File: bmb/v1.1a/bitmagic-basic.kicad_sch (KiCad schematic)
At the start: 39 parts, among them IC1 CY7C68013A-56, J1 Conn, J2 USB_C_Receptacle_USB2.0, U1 3.3V, U2 USBLC6-2, U3 IP425x-4-TTL, U4 IP425x-4-TTL, U5 24LC00, U6 IP425x-4-TTL, X1 24MHz

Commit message: bmb: Updated manufacturing data.
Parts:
- C14: Key cap-cer-0401-1u -> cap-cer-0402-1u
- D1: MFN (none) -> ORH-G36A; Manufacturer (none) -> Orient
- IC1: MFN (none) -> CY768013A-56; Manufacturer (none) -> Cypress
- J2: Key (none) -> conn-smd-usb-c-2; MFN (none) -> TYPE-C-31-M-12; Manufacturer (none) -> Korean Horoparts; Source (none) -> ANY
- R1: value 330E -> 2k7; Key res-0402-330 -> res-0402-2k7
- U1: MFN (none) -> SPX3819M5-L-3-3/TR; Manufacturer (none) -> MaxLinear
- U2: MFN (none) -> USBLC6-2P6; Manufacturer (none) -> STM
- U3, U4, U6: MFN (none) -> IP4254CZ8-4-TTL; Manufacturer (none) -> Nexperia
- U5: MFN (none) -> 24LC00T-I/OT; Manufacturer (none) -> Microchip
- X1: MFN (none) -> JF4024M00009T8188070; Manufacturer (none) -> JWT

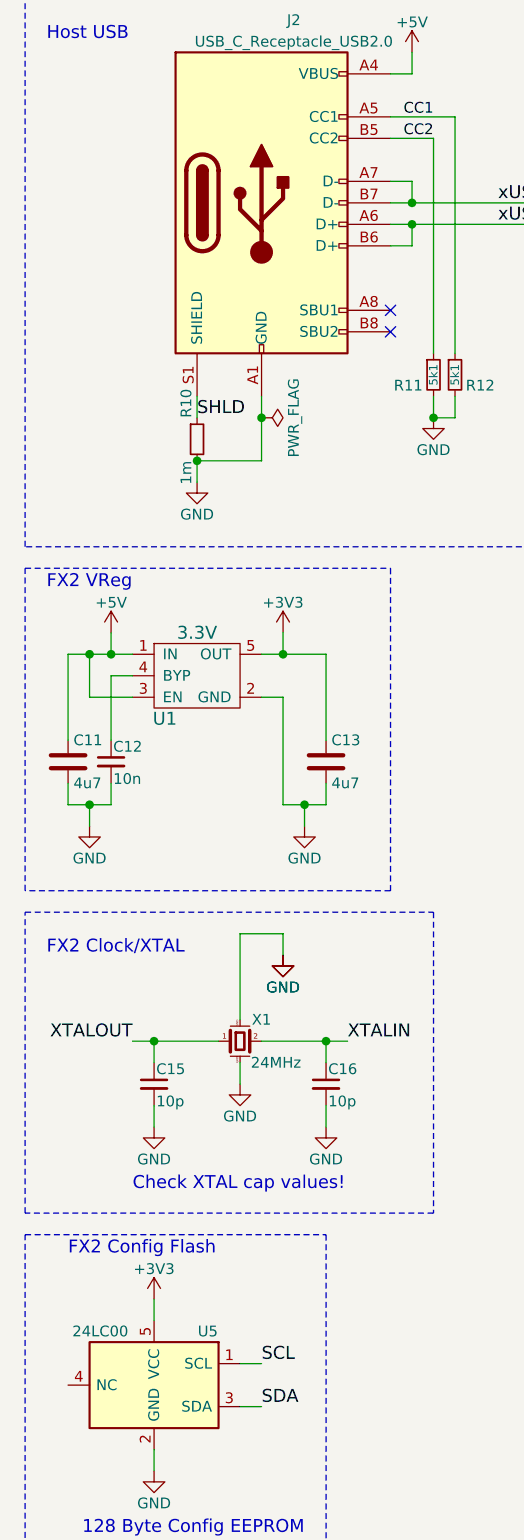
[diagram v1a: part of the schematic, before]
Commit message: Upgrade to new KiCad file formats
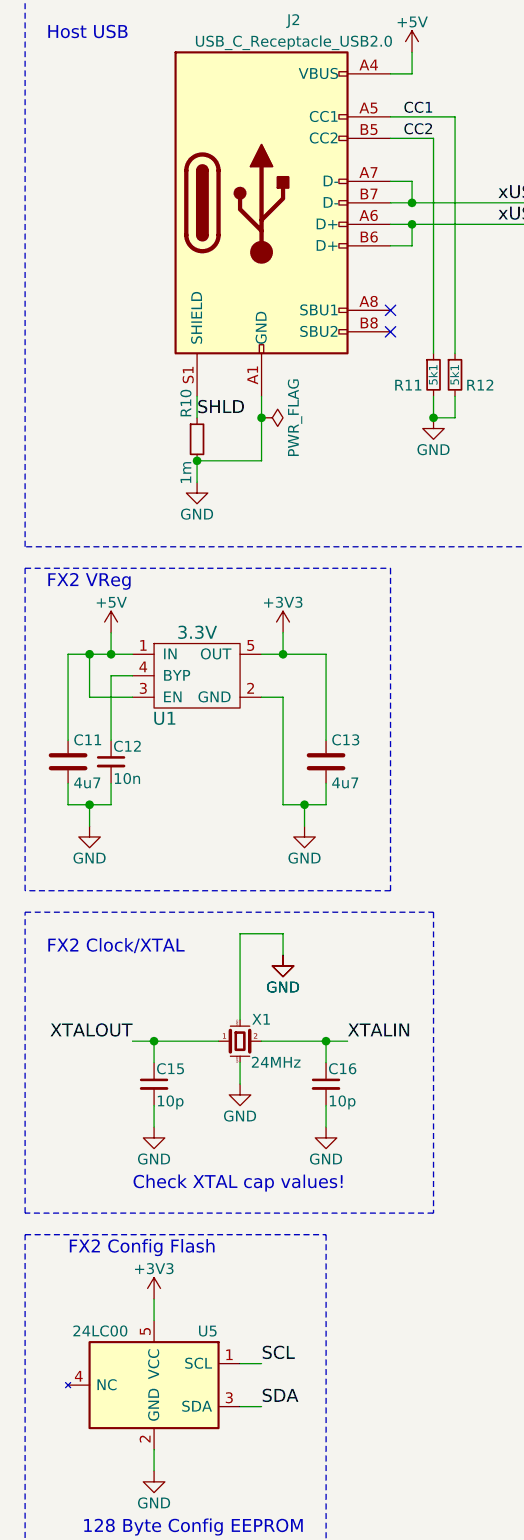
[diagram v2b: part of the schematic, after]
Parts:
- IC1: MFN CY768013A-56 -> (none)
- U1: MFN SPX3819M5-L-3-3/TR -> (none)
- U2: MFN USBLC6-2P6 -> (none)
- U3, U4, U6: MFN IP4254CZ8-4-TTL -> (none)
- U5: MFN 24LC00T-I/OT -> (none)
- X1: MFN JF4024M00009T8188070 -> (none)
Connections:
- net ~RESET renamed ~{RESET}

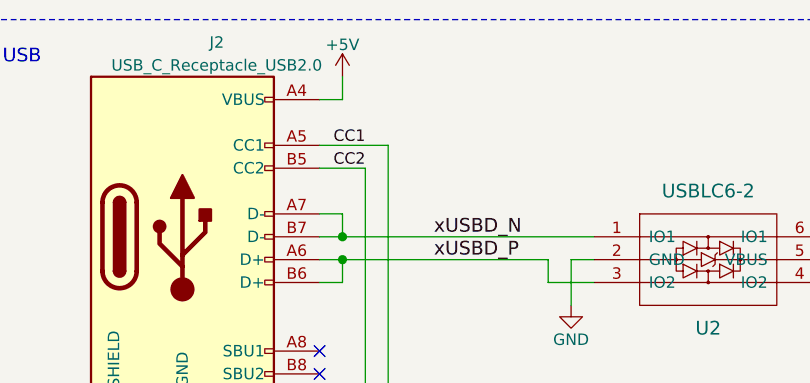
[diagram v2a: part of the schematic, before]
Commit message: Add PWR_FLAG to soothe ERC
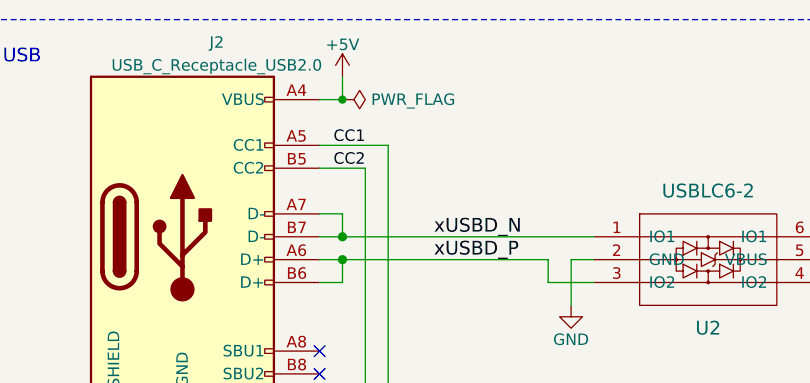
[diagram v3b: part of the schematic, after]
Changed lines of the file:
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@@
   (junction (at 147.32 30.48) (diameter 1.016) (color 0 0 0 0)
   )
+  (junction (at 58.42 21.59) (diameter 0) (color 0 0 0 0)
+  )
   (junction (at 157.48 40.64) (diameter 1.016) (color 0 0 0 0)
   )
@@
     (pin "1")
   )
+  (symbol (lib_id "power:PWR_FLAG") (at 58.42 21.59 270) (unit 1)
+    (in_bom yes) (on_board yes)
+    (property "Reference" "#FLG0101" (id 0) (at 60.325 21.59 0)
+      (effects (font (size 1.27 1.27)) hide)
+    )
+    (property "Value" "PWR_FLAG" (id 1) (at 61.595 21.59 90)
+      (effects (font (size 1.27 1.27)) (justify left))
+    )
+    (property "Footprint" "" (id 2) (at 58.42 21.59 0)
+      (effects (font (size 1.27 1.27)) hide)
+    )
+    (property "Datasheet" "~" (id 3) (at 58.42 21.59 0)
+      (effects (font (size 1.27 1.27)) hide)
+    )
+    (pin "1")
+  )
   (symbol (lib_id "Connector:USB_C_Receptacle_USB2.0") (at 40.64 36.83 0) (unit 1)
     (in_bom yes) (on_board yes)
@@
       (reference "#FLG030") (unit 1) (value "PWR_FLAG") (footprint "")
     )
+    (path "/3a3ce4ec-789c-4548-ae20-37d3967597c0"
+      (reference "#FLG0101") (unit 1) (value "PWR_FLAG") (footprint "")
+    )
     (path "/00000000-0000-0000-0000-000059bc78f7"
